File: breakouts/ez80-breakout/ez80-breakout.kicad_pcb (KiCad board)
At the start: 4 copper layers, 30.5 x 142.2 mm, 30 parts, among them J1 PORTD, J10 IRQ & Mem, J11 ~INSTRD, J12 ~WAIT, J13 ~BUSREQACK, J14 ~NMI, J15 ZDI, J16 TRIGOUT, J17 PHI, J18 PORTB, J19 VDD, J2 PORTC, J20 RTC_VDD, J21 GND, J3 ADDR[0..23], J4 I2C, J5 RTC_XINOUT, J6 XINOUT, J7 ~RESET, J8 DATA[0..7], J9 ~CS[0..3], U1 EZ80L92AZ050SG

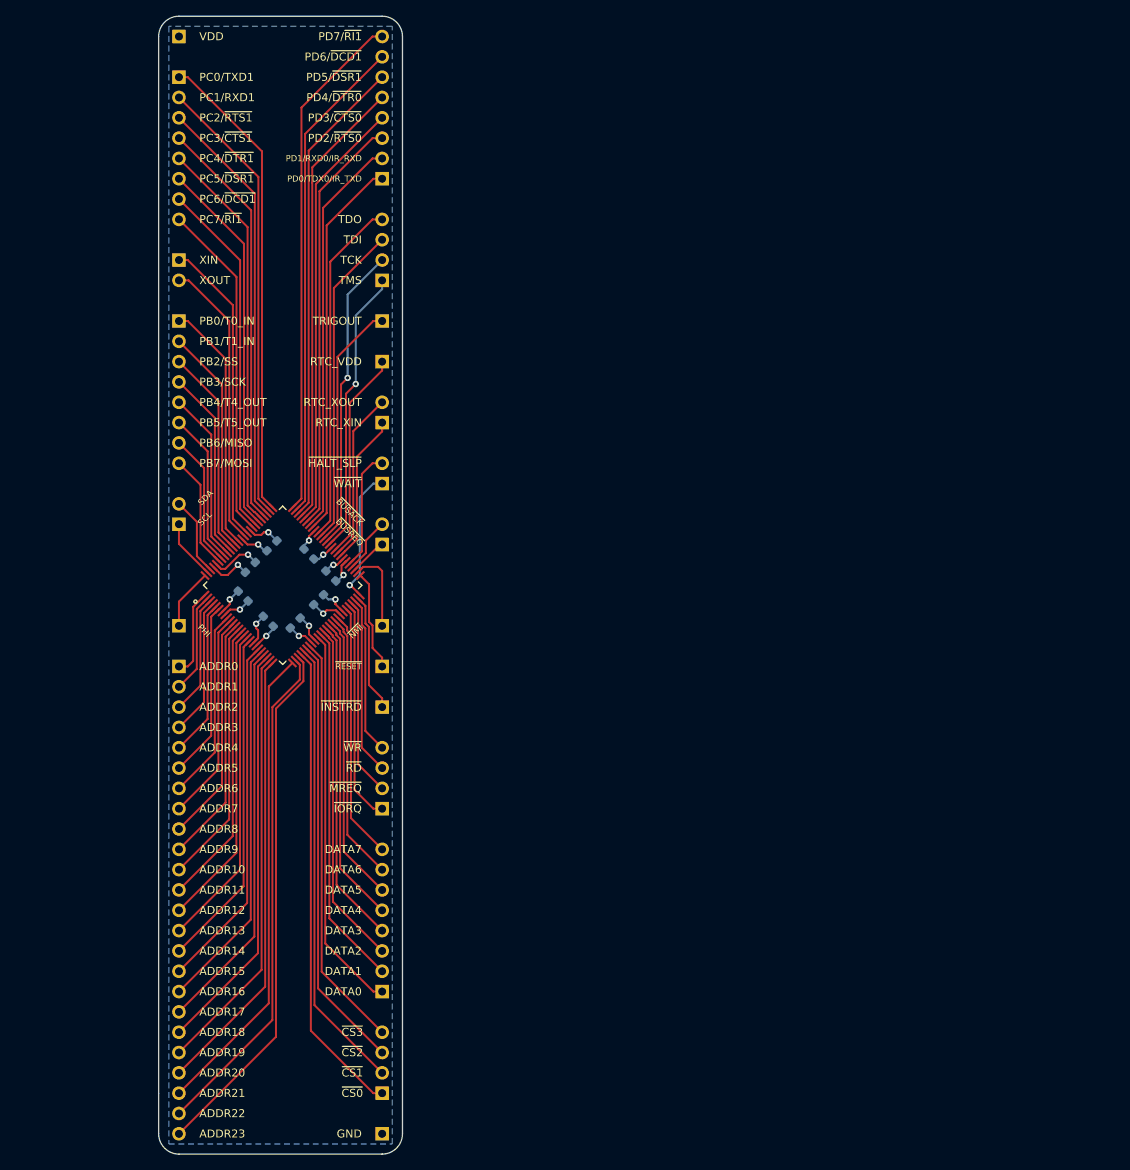
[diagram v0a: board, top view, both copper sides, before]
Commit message: ez80 breakout: Create a breadboard compatible eZ80 Breakout
Additionally:
  - Import the OSHW logo
  - Draw up SO-8 footprint for the opto-isolators
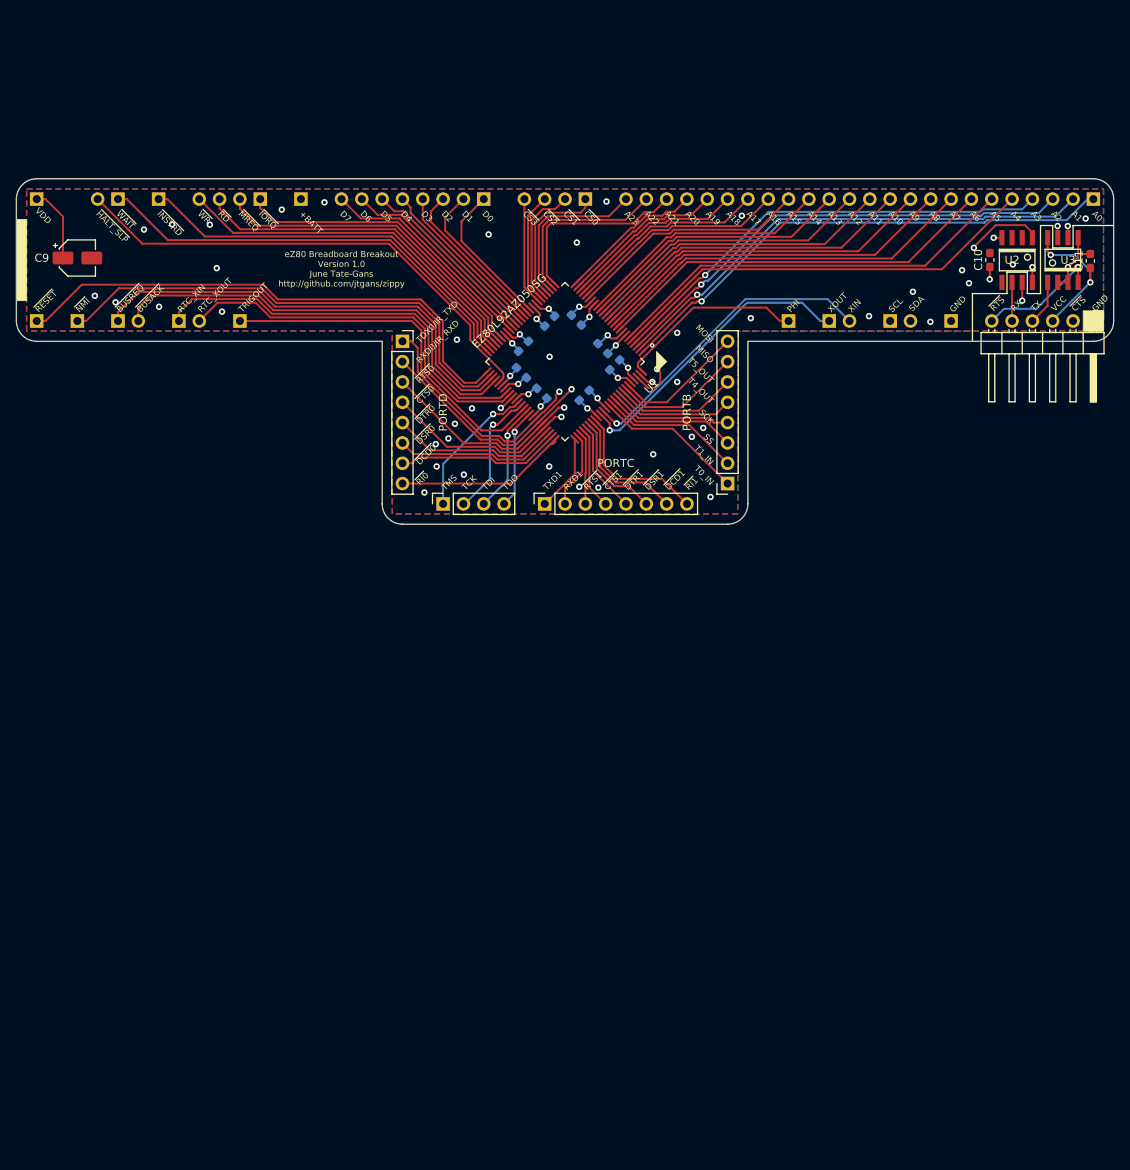
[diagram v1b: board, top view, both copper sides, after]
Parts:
- added C10: 10nF, Capacitor_SMD:C_0603_1608Metric_Pad1.05x0.95mm_HandSolder, F.Cu at (200.4, 60.9)
- added C11: 10nF, Capacitor_SMD:C_0603_1608Metric_Pad1.05x0.95mm_HandSolder, F.Cu at (213.0, 61.1)
- added C9: 1uF, Capacitor_SMD:CP_Elec_4x4.5, F.Cu at (86.4, 60.7)
- added G***: LOGO, footprints:oshw_small, B.Cu at (118.7, 62.2)
- added J22: TTY, Connector_PinHeader_2.54mm:PinHeader_1x06_P2.54mm_Horizontal, F.Cu at (213.4, 68.6)
- added U2: BB Powered, footprints:SO-8, F.Cu at (203.8, 61.0)
- added U3: PC Powered, footprints:SO-8, F.Cu at (209.6, 61.0)
- J1, J18, J2: footprint Connector_PinHeader_2.54mm:PinHeader_1x08_P2.54mm_Vertical -> Connector_PinSocket_2.54mm:PinSocket_1x08_P2.54mm_Vertical; moved to F.Cu
- J15: footprint Connector_PinHeader_2.54mm:PinHeader_1x04_P2.54mm_Vertical -> Connector_PinSocket_2.54mm:PinSocket_1x04_P2.54mm_Vertical; moved to F.Cu
- moved J3 128.4 mm to (213.4, 53.3), turned to 90 degrees
- moved J21 124.0 mm to (195.6, 68.6), turned to 270 degrees
- moved J9 114.6 mm to (149.9, 53.3), turned to 90 degrees
- moved J8 99.9 mm to (137.2, 53.3), turned to 90 degrees
- moved J4 92.5 mm to (188.0, 68.6), turned to 270 degrees
- moved J17 85.2 mm to (175.3, 68.6), turned to 270 degrees
- moved J6 81.6 mm to (180.3, 68.6), turned to 270 degrees
- moved J10 77.7 mm to (109.2, 53.3), turned to 90 degrees
- moved J18 71.5 mm to (167.6, 88.9)
- moved J2 70.3 mm to (144.8, 91.4), turned to 90 degrees
- moved J11 69.4 mm to (96.5, 53.3), turned to 270 degrees
- moved J7 61.1 mm to (81.3, 68.6), turned to 270 degrees
- moved C1 54.1 mm to (148.7, 68.5), turned to 315 degrees
- moved J14 53.9 mm to (86.4, 68.6), turned to 270 degrees
- moved J12 48.5 mm to (91.4, 53.3), turned to 90 degrees
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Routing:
- net /~RESET: track 12.5 -> 66.8 mm
- net /ADDR0: track 10.9 -> 64.2 mm, vias 0 -> 1
- net /~BUSREQ: track 4.75 -> 57.7 mm
- net /~NMI: track 10.5 -> 61.9 mm
- net /PD1: track 50.2 -> 100.3 mm, vias 0 -> 2
- net /PC0: track 59.3 -> 9.67 mm
- net /ADDR1: track 12.6 -> 61.9 mm, vias 0 -> 1
- net /~BUSACK: track 6.93 -> 55.7 mm
- net /~HALT_SLP: track 15.0 -> 62.2 mm
- net /PD3: track 54.2 -> 101.2 mm, vias 0 -> 2
- net /PC1: track 56.3 -> 9.55 mm
- net /PD0: track 47.9 -> 94.5 mm, vias 0 -> 2
- net /PD2: track 52.6 -> 98.9 mm, vias 0 -> 2
- net /ADDR23: track 66.3 -> 20.9 mm
- net /PC2: track 54.0 -> 9.08 mm
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- added copper zone on In2.Cu, net +3V3
- added copper zone on F.Cu, net GND
- added copper zone on In1.Cu, net GND
- removed copper zone on In1.Cu, net +3V3
- removed copper zone on In2.Cu, net GND
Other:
- board size 30.5 x 142.2 mm -> 137.2 x 43.2 mm
- rule pad_to_mask_clearance: 0.051 -> 0.0508
- board text added: "+BATT"
- board text added: "A0"
- board text added: "A1"
- board text added: "A10"
- board text added: "A11"
- board text added: "A12"
- board text added: "A13"
- board text added: "A14"
- board text added: "A15"
- board text added: "A16"
- board text added: "A17"
- board text added: "A18"
- board text added: "A19"
- board text added: "A2"
- board text added: "A20"
- board text added: "A21"
- board text added: "A22"
- board text added: "A23"
- board text added: "A3"
- board text added: "A4"
- board text added: "A5"
- board text added: "A6"
- board text added: "A7"
- board text added: "A8"
- board text added: "A9"
- board text added: "D0"
- board text added: "D1"
- board text added: "D2"
- board text added: "D3"
- board text added: "D4"
- board text added: "D5"
- board text added: "D6"
- board text added: "D7"
- board text added: "GND"
- board text added: "MISO"
- board text added: "MOSI"
- board text added: "PHI"
- board text added: "RX"
- board text added: "RXD0/IR_RXD"
- board text added: "RXD1"
- board text added: "SCK"
- board text added: "SS"
- board text added: "T0_IN"
- board text added: "T1_IN"
- board text added: "T4_OUT"
- board text added: "T5_OUT"
- board text added: "TDX0/IR_TXD"
- board text added: "TRIGOUT"
- board text added: "TX"
- board text added: "TXD1"
- board text added: "VCC"
- board text added: "eZ80 Breadboard Breakout Version 1.0 June Tate-Gans http://github.com/jtgans/zippy"
- board text added: "~CTS"
- board text added: "~CTS0"
- board text added: "~CTS1"
- board text added: "~DCD0"
- board text added: "~DCD1"
- board text added: "~DSR0"
- board text added: "~DSR1"
- board text added: "~DTR0"
- board text added: "~DTR1"
- board text added: "~INSTRD"
- board text added: "~NMI"
- board text added: "~RESET"
- board text added: "~RI0"
- board text added: "~RI1"
- board text added: "~RTS"
- board text added: "~RTS0"
- board text added: "~RTS1"
- board text removed: "ADDR0"
- board text removed: "ADDR1"
- board text removed: "ADDR10"
- board text removed: "ADDR11"
- board text removed: "ADDR12"
- board text removed: "ADDR13"
- board text removed: "ADDR14"
- board text removed: "ADDR15"
- board text removed: "ADDR16"
- board text removed: "ADDR17"
- board text removed: "ADDR18"
- board text removed: "ADDR19"
- board text removed: "ADDR2"
- board text removed: "ADDR20"
- board text removed: "ADDR21"
- board text removed: "ADDR22"
- board text removed: "ADDR23"
- board text removed: "ADDR3"
- board text removed: "ADDR4"
- board text removed: "ADDR5"
- board text removed: "ADDR6"
- board text removed: "ADDR7"
- board text removed: "ADDR8"
- board text removed: "ADDR9"
- board text removed: "DATA0"
- board text removed: "DATA1"
- board text removed: "DATA2"
- board text removed: "DATA3"
- board text removed: "DATA4"
- board text removed: "DATA5"
- board text removed: "DATA6"
- board text removed: "DATA7"
- board text removed: "PB0/T0_IN"
- board text removed: "PB1/T1_IN"
- board text removed: "PB2/SS"
- board text removed: "PB3/SCK"
- board text removed: "PB4/T4_OUT"
- board text removed: "PB5/T5_OUT"
- board text removed: "PB6/MISO"
- board text removed: "PB7/MOSI"
- board text removed: "PC0/TXD1"
- board text removed: "PC1/RXD1"
- board text removed: "PC2/~RTS1"
- board text removed: "PC3/~CTS1"
- board text removed: "PC4/~DTR1"
- board text removed: "PC5/~DSR1"
- board text removed: "PC6/~DCD1"
- board text removed: "PC7/~RI1"
- board text removed: "PD0/TDX0/IR_TXD"
- board text removed: "PD1/RXD0/IR_RXD"
- board text removed: "PD2/~RTS0"
- board text removed: "PD3/~CTS0"
- board text removed: "PD4/~DTR0"
- board text removed: "PD5/~DSR1"
- board text removed: "PD6/~DCD1"
- board text removed: "PD7/~RI1"
- board text removed: "eZ80 Breadboard Breakout Version 1.0 June Tate-Gans"
